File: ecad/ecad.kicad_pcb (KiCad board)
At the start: 2 copper layers, 151.1 x 151.1 mm, 27 parts, among them J1 Conn_01x03_Female, J10 Conn_01x05_Female, J4 Conn_01x03_Female, J5 Conn_01x03_Female, J6 Conn_01x03_Female, J7 Conn_01x05_Female, J8 Conn_01x05_Female, J9 Conn_01x05_Female, U1 DHT11, U2 ABX00012

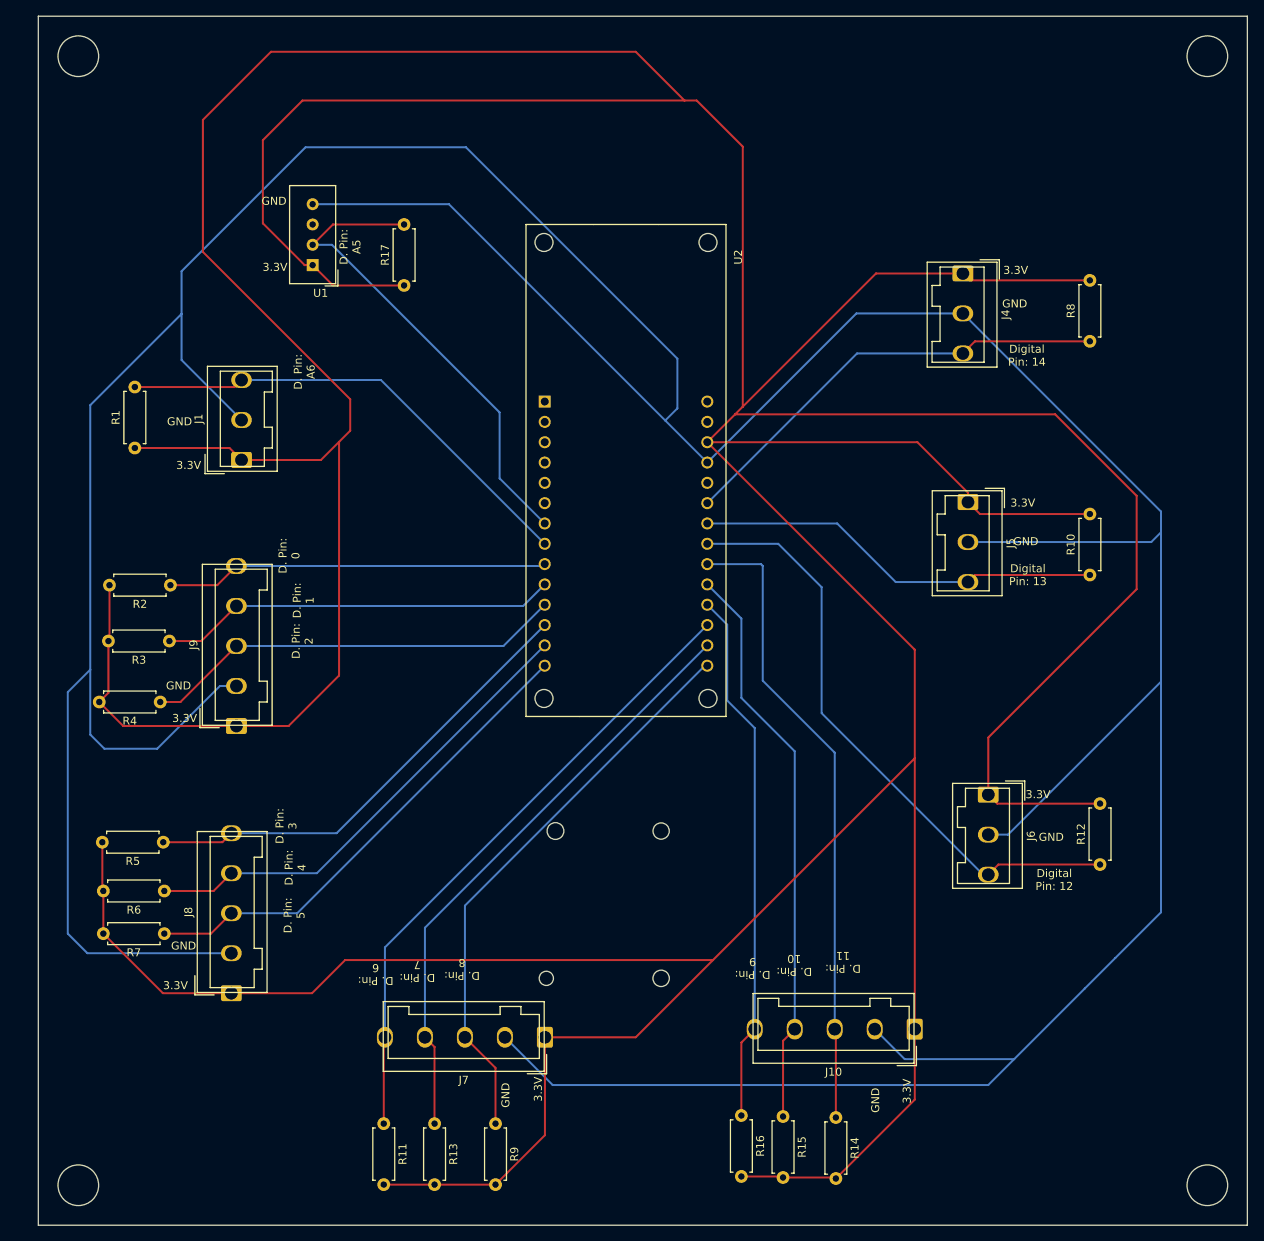
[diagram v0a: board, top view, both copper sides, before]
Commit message: make pcb smaller and only one wire for each cable
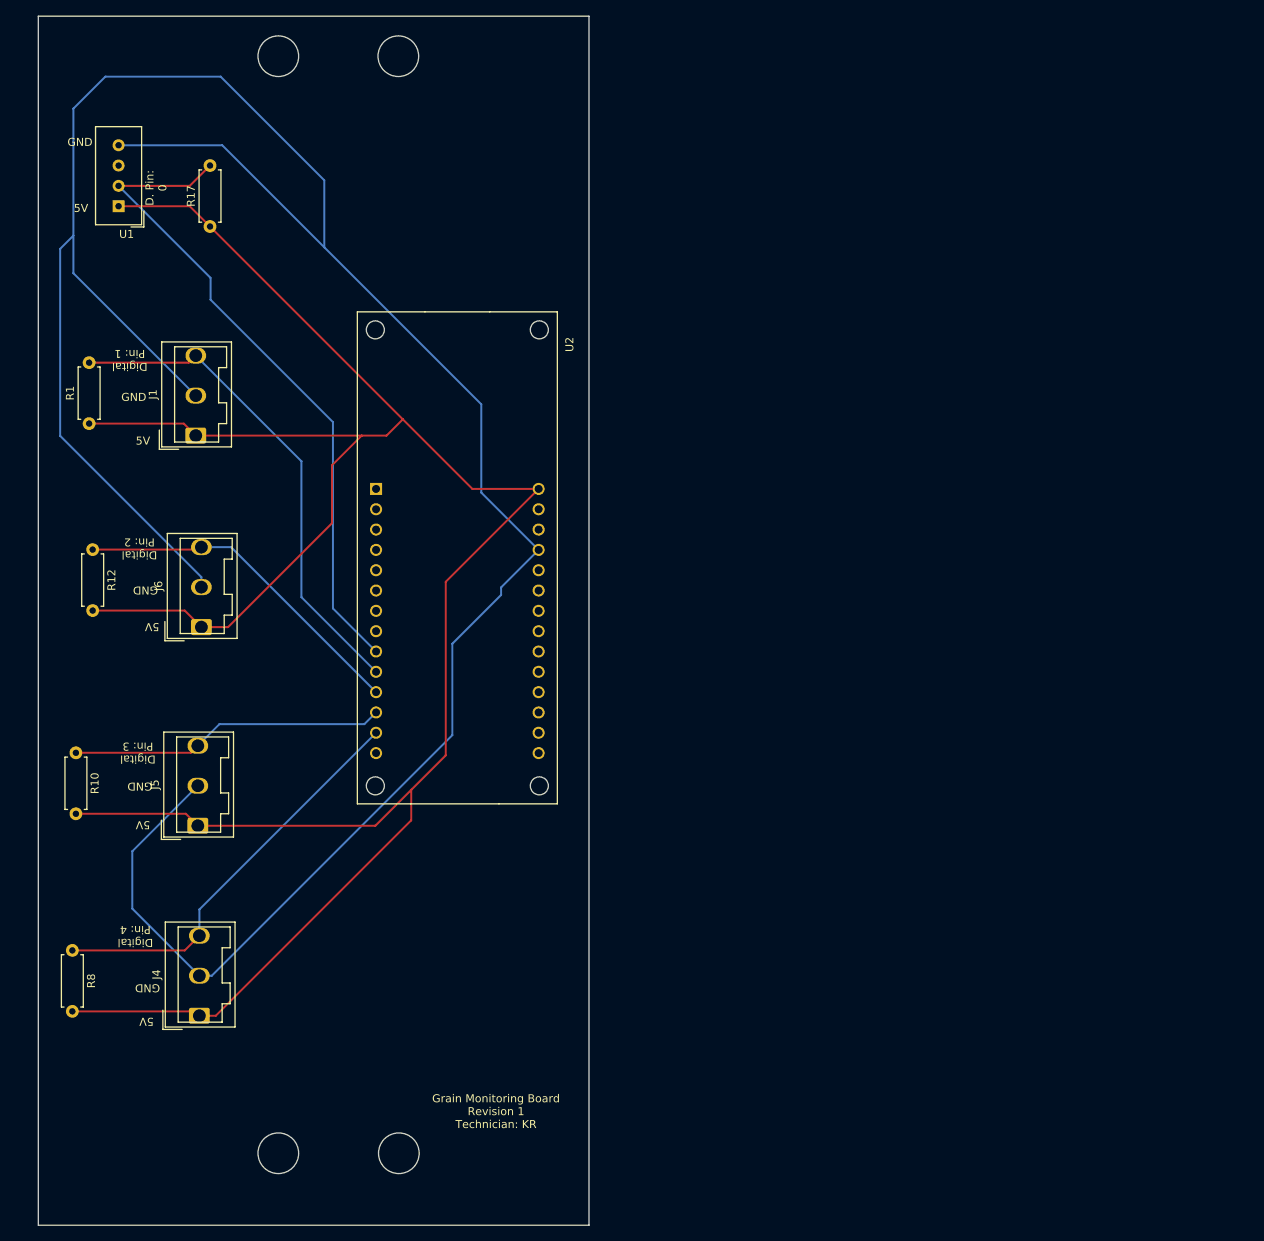
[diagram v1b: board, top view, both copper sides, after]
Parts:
- removed J10, J7, J8, J9: Conn_01x05_Female, digikey-footprints:Wago_734-135_1x05_P5.0mm_Vertical
- removed R11, R13, R14, R15, R16, R2, R3, R4, R5, R6, R7, R9: 10K, Resistor_THT:R_Axial_DIN0207_L6.3mm_D2.5mm_P7.62mm_Horizontal
- U1: value DHT11 -> DHT22
- moved R8 148.2 mm to (51.2, 143.4), turned to 270 degrees
- moved R12 131.9 mm to (53.8, 93.3), turned to 270 degrees
- moved J4 131.0 mm to (67.1, 150.1), turned to 90 degrees
- moved R10 128.7 mm to (51.7, 118.7), turned to 270 degrees
- moved J5 103.3 mm to (66.9, 126.4), turned to 90 degrees
- moved J6 101.2 mm to (67.4, 101.5), turned to 90 degrees
- moved U1 25.4 mm to (57.0, 50.4)
- moved R17 25.4 mm to (68.5, 53.0)
- moved U2 23.7 mm to (86.9, 63.6)
- moved J1 6.48 mm to (66.7, 77.6)
- moved R1 6.48 mm to (53.3, 77.6)
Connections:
- U2 pad 10: Net-(J9-Pad4) -> Net-(J1-Pad3)
- U2 pad 11: Net-(J9-Pad3) -> Net-(J6-Pad3)
- U2 pad 12: Net-(J8-Pad5) -> Net-(J5-Pad3)
- U2 pad 13: Net-(J8-Pad4) -> Net-(J4-Pad3)
- U2 pad 21: Net-(J6-Pad3) -> Net-(U2-Pad21)
- U2 pad 22: Net-(J5-Pad3) -> Net-(U2-Pad22)
- U2 pad 23: Net-(J4-Pad3) -> Net-(U2-Pad23)
- U2 pad 26: +VDC -> Net-(U2-Pad26)
- U2 pad 28: Net-(U2-Pad28) -> +VDC
- U2 pad 7: Net-(R17-Pad2) -> Net-(U2-Pad7)
- U2 pad 8: Net-(J1-Pad3) -> Net-(U2-Pad8)
- U2 pad 9: Net-(J9-Pad5) -> Net-(R17-Pad2)
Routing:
- net +VDC: track 878.1 -> 301.6 mm
- net -VDC: track 598.6 -> 323.2 mm
- net Net-(U2-Pad20): track 79.8 -> 0.00 mm
- net Net-(U2-Pad17): track 79.1 -> 0.00 mm
- net Net-(U2-Pad16): track 74.9 -> 0.00 mm
- net Net-(U2-Pad19): track 71.6 -> 0.00 mm
- net Net-(U2-Pad15): track 71.6 -> 0.00 mm
- net Net-(U2-Pad18): track 67.0 -> 0.00 mm
- net Net-(U2-Pad14): track 61.4 -> 0.00 mm
- net Net-(J8-Pad4): track 60.3 -> 0.00 mm
- net Net-(J8-Pad5): track 58.9 -> 0.00 mm
- net Net-(J9-Pad3): track 53.1 -> 0.00 mm
- net Net-(J9-Pad4): track 49.8 -> 0.00 mm
- net Net-(J9-Pad5): track 47.9 -> 0.00 mm
- net Net-(J6-Pad3): track 76.0 -> 43.1 mm
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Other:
- board size 151.1 x 151.1 mm -> 68.8 x 151.1 mm
- board text added: "5V"
- board text added: "Digital Pin: 1"
- board text added: "Digital Pin: 2"
- board text added: "Digital Pin: 3"
- board text added: "Digital Pin: 4"
- board text added: "Grain Monitoring Board Revision 1 Technician: KR"
- board text removed: "3.3V"
- board text removed: "D. Pin: 1"
- board text removed: "D. Pin: 10"
- board text removed: "D. Pin: 11"
- board text removed: "D. Pin: 2"
- board text removed: "D. Pin: 3"
- board text removed: "D. Pin: 4"
- board text removed: "D. Pin: 5"
- board text removed: "D. Pin: 6"
- board text removed: "D. Pin: 7"
- board text removed: "D. Pin: 8"
- board text removed: "D. Pin: 9"
- board text removed: "D. Pin: A5"
- board text removed: "D. Pin: A6"
- board text removed: "Digital Pin: 12"
- board text removed: "Digital Pin: 13"
- board text removed: "Digital Pin: 14"

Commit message: update pcb board
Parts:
- added G***: LOGO, custom_libraries:farm_hacks_logo, F.Cu at (102.1, 146.3)

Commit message: updated pcb to use 3.3V instead of 5V
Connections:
- U2 pad 26: Net-(U2-Pad26) -> +VDC
- U2 pad 28: +VDC -> Net-(U2-Pad28)
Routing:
- net +VDC: track 301.6 -> 295.9 mm
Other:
- board text added: "3.3V"
- board text added: "Grain Monitoring Board Revision 2 Technician: KR"
- board text removed: "5V"
- board text removed: "Grain Monitoring Board Revision 1 Technician: KR"

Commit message: add resistor values to silkscreen
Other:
- board text added: "10K Ohm"
- board text added: "For DS18B20 (cable sensors) resistors use 4.7 K Ohm: Close by bins (board directly under or beside) 560 Ohm: Far away bins"
